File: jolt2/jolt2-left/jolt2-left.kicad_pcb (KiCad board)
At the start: 2 copper layers, 147 x 98 mm, 62 parts, among them J1 Conn_01x02_Pin, J10 Conn_01x02_Pin, J11 Conn_01x02_Pin, J12 Conn_01x02_Pin, J13 Conn_01x02_Pin, J14 Conn_01x02_Pin, J15 Conn_01x02_Pin, J16 Conn_01x02_Pin, J17 Conn_01x02_Pin, J18 Conn_01x02_Pin, J19 Conn_01x02_Pin, J2 Conn_01x02_Pin, J20 Conn_01x02_Pin, J21 Conn_01x02_Pin, J22 Conn_01x02_Pin, J23 Conn_01x02_Pin, J24 Conn_01x02_Pin, J25 Conn_01x02_Pin, J26 Conn_01x02_Pin, J27 Conn_01x02_Pin, J28 Conn_01x02_Pin, J29 USB_C_Receptacle_USB2.0_14P, J3 Conn_01x02_Pin, J30 Conn_ARM_JTAG_SWD_10, J4 Conn_01x02_Pin, J5 Conn_01x02_Pin, J6 Conn_01x02_Pin, J7 Conn_01x02_Pin, J8 Conn_01x02_Pin, J9 Conn_01x02_Pin, SW1 SW_SPST, SW2 SW_SPST, U1 RP2040, U3 W25Q128JVP, Y1 ABM8-272-T3

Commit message: jolt2: Prepare rev A
This is Rev A, being sent for production.
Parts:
- added J31: RJ45, Connector_RJ:RJ45_Amphenol_54602-x08_Horizontal, F.Cu at (173.8, 138.0)
- J29: footprint Connector_USB:USB_C_Receptacle_GCT_USB4085 -> davidb-keyboard-foot:USB_C_Receptacle_GCT_USB4085
- moved J30 12.8 mm to (177.2, 148.6)
- moved C9 3.30 mm to (171.5, 124.2)
- moved C11 0.40 mm to (157.1, 123.5)
- moved R3 0.10 mm to (157.1, 107.5)
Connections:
- U1 pad 2: /COL-A -> /COL-C
- U1 pad 4: /COL-C -> /COL-A
- U1 pad 40: unconnected-(U1-GPIO28_ADC2-Pad40) -> SERTX
- U1 pad 41: unconnected-(U1-GPIO29_ADC3-Pad41) -> SERRX
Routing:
- net /ROW-A: track 0.00 -> 228.4 mm, vias 0 -> 1
- net /ROW-D: track 0.00 -> 153.2 mm, vias 0 -> 2
- net /ROW-B: track 0.00 -> 145.6 mm
- net /ROW-C: track 0.00 -> 143.6 mm
- net /COL-A: track 0.00 -> 139.6 mm
- net /ROW-F: track 0.00 -> 120.1 mm, vias 0 -> 1
- net /ROW-E: track 0.00 -> 110.0 mm, vias 0 -> 2
- net /COL-B: track 0.00 -> 109.6 mm
- net /COL-C: track 0.00 -> 87.3 mm
- net +3.3V: track 103.3 -> 162.2 mm, vias 4 -> 8
- net RUN: track 18.6 -> 74.7 mm, vias 2 -> 4
- net /COL-D: track 0.00 -> 49.1 mm, vias 0 -> 1
- net VBUS: track 7.49 -> 51.5 mm, vias 0 -> 1
- net SERRX: track 0.00 -> 19.9 mm, vias 0 -> 1
- net SERTX: track 0.00 -> 15.7 mm, vias 0 -> 1
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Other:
- board size 147 x 98 mm -> 151 x 98 mm
- board text added: "Jolt 2 - Left REV A"

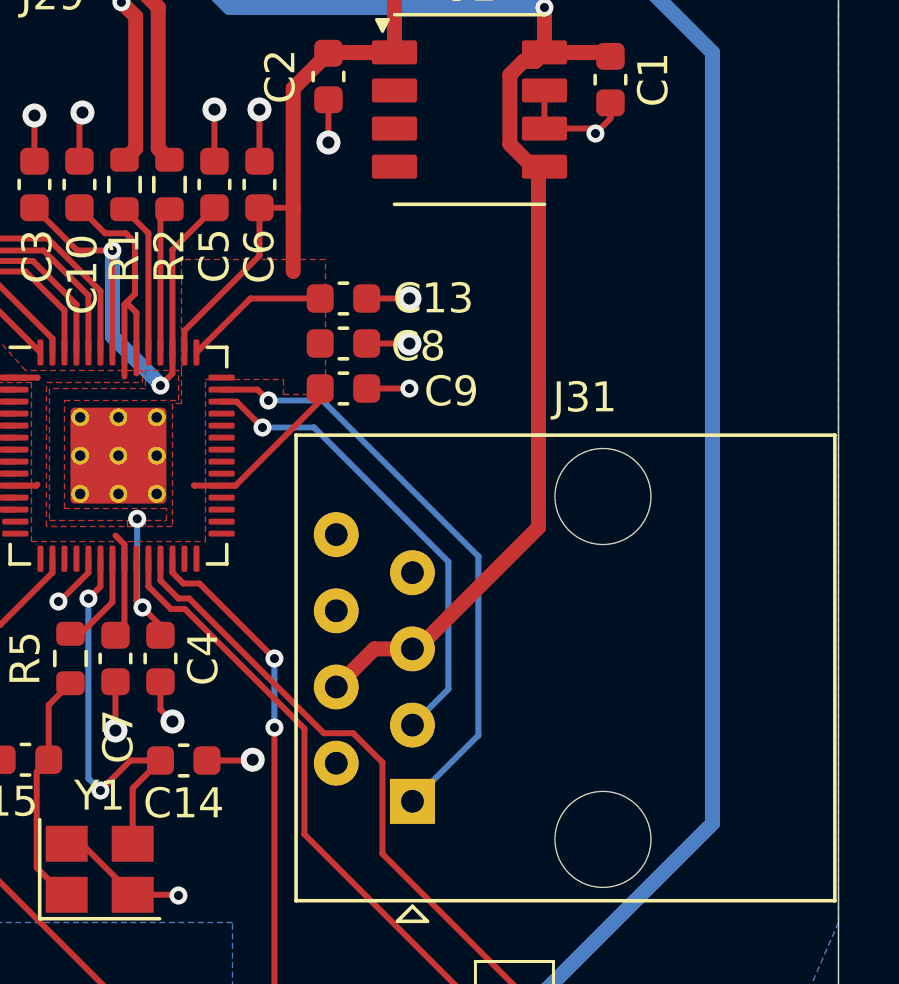
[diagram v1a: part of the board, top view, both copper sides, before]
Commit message: jolt2-left: Add inter-board termination
Add 27 ohm resisters for termination on the inter-board protocol.
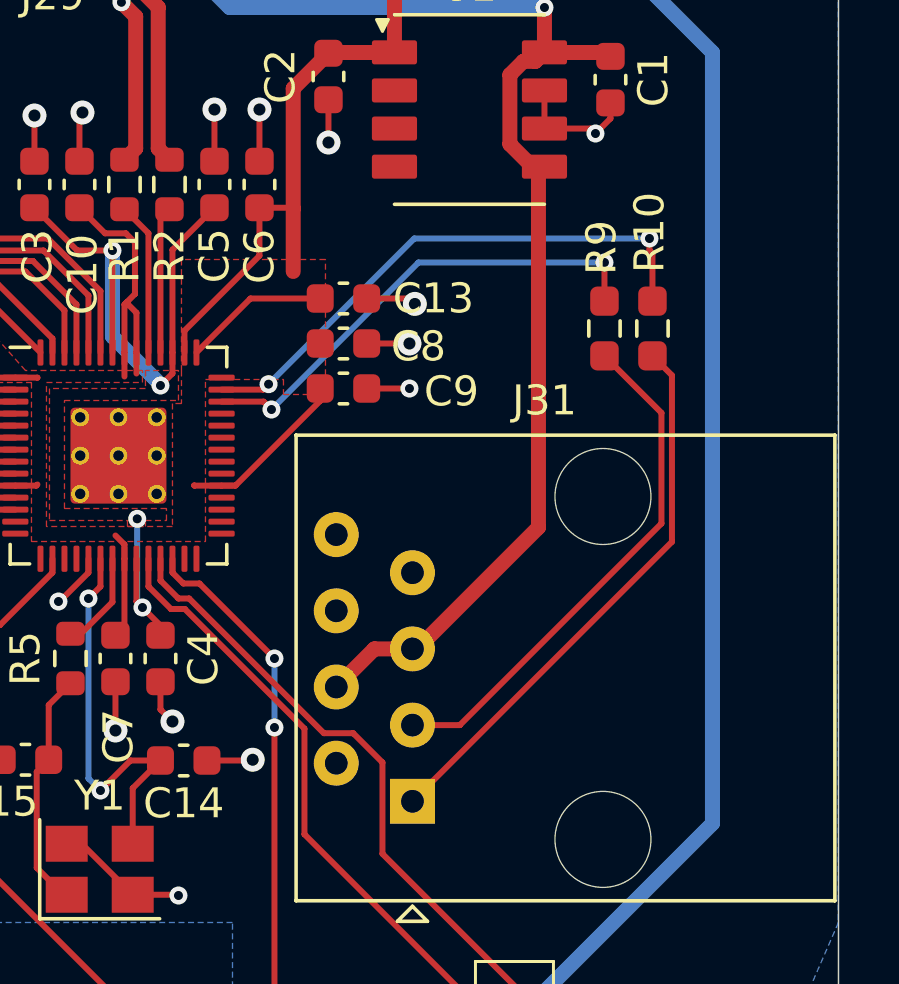
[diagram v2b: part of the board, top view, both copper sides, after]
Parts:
- added R10: 27, Resistor_SMD:R_0603_1608Metric_Pad0.98x0.95mm_HandSolder, F.Cu at (181.8, 122.2)
- added R9: 27, Resistor_SMD:R_0603_1608Metric_Pad0.98x0.95mm_HandSolder, F.Cu at (180.2, 122.2)
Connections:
- J31 pad 1: SERRX -> Net-(J31-Pad1)
- J31 pad 3: SERTX -> Net-(J31-Pad3)
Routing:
- net Net-(J31-Pad1): track 0.00 -> 18.7 mm
- net Net-(J31-Pad3): track 0.00 -> 17.5 mm
- net SERRX: track 19.9 -> 18.5 mm, vias 1 -> 2
- net SERTX: track 15.7 -> 16.2 mm, vias 1 -> 2

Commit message: Various PCB updates
This is before fixing the footprint for the WS2812. Turns out there is a
ws2812 MINI, and a MINI-HS, and they have very different footprints.
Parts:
- C14, C15: value 1u -> 12p
- C16: value C -> 100n
- R3, R4: value R -> 5.1k
- U2: value ~ -> AP2112-M3.3

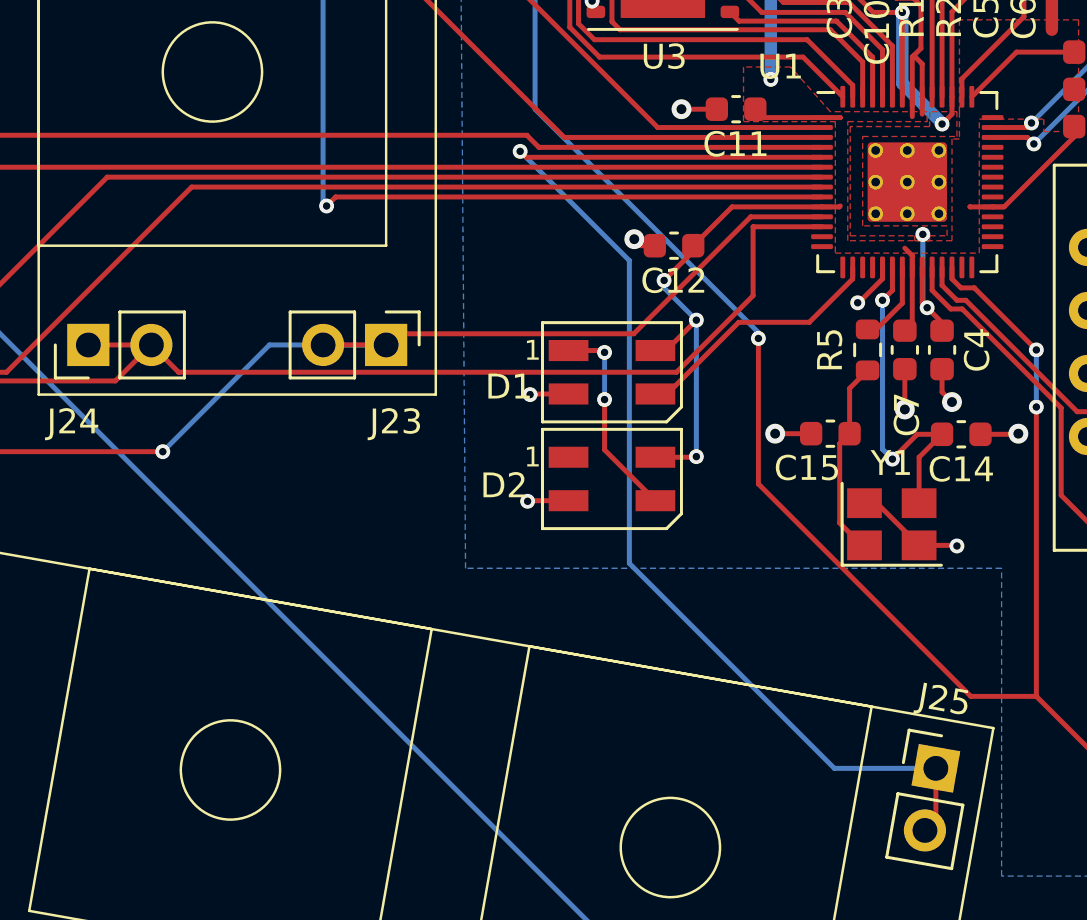
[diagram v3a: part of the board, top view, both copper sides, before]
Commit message: jolt2-left: Fix symbol and footprint for ws2812
The ws2812 has both a MINI and a MINI-HS footprint, and they have rather
different footprints.  Update the symbol and draw a footprint for the
proper one we have purchased.
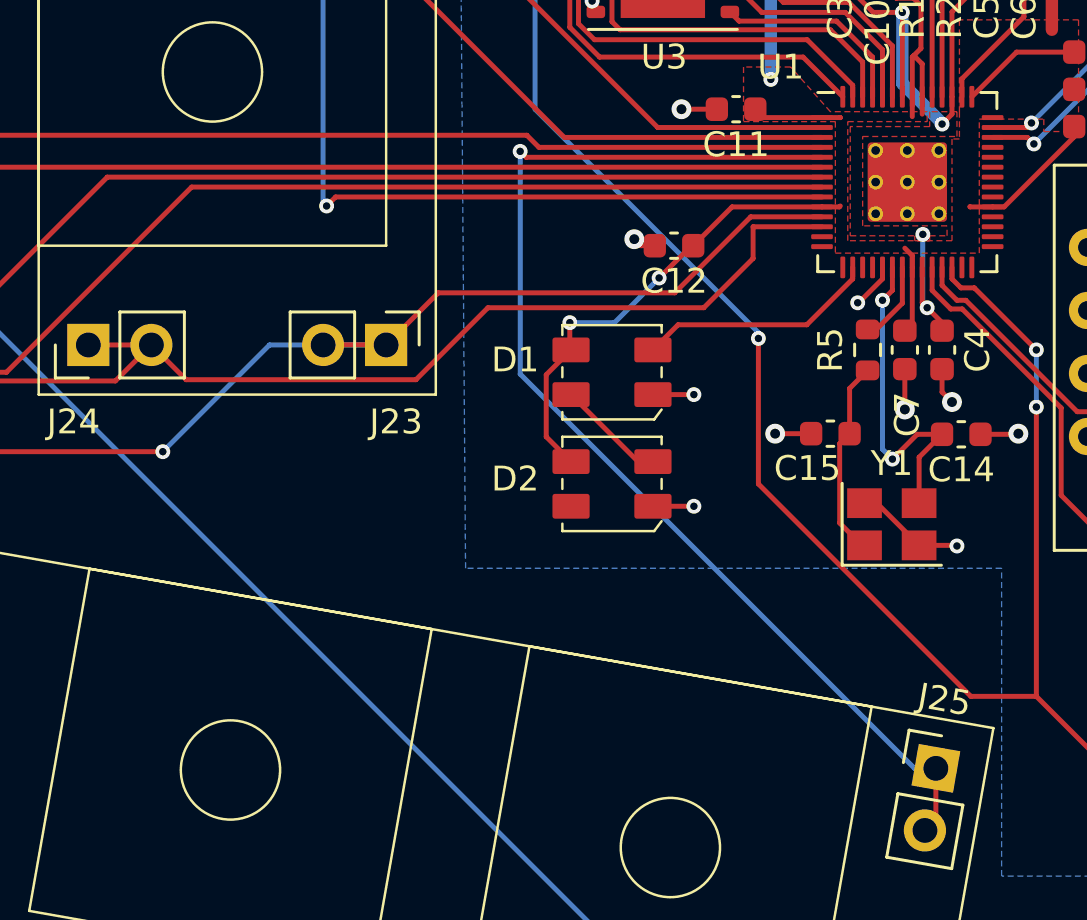
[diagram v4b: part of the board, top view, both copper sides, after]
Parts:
- D1, D2: value SK6812MINI -> SK6812MINI-HS; footprint LED_SMD:LED_SK6812MINI_PLCC4_3.5x3.5mm_P1.75mm -> davidb-keyboard-foot:SK6812-MINI-HS
- moved D2 0.20 mm to (152.1, 138.6), turned to 180 degrees
- turned D1 to 180 degrees
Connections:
- D1 pad 1: Net-(D1-DOUT) -> GND
- D1 pad 2: GND -> RGB
- D1 pad 3: RGB -> +3.3V
- D1 pad 4: +3.3V -> Net-(D1-DOUT)
- D2 pad 1: unconnected-(D2-DOUT-Pad1) -> GND
- D2 pad 2: GND -> Net-(D1-DOUT)
- D2 pad 3: Net-(D1-DOUT) -> +3.3V
- D2 pad 4: +3.3V -> unconnected-(D2-DOUT-Pad4)
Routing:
- net Net-(D1-DOUT): track 8.31 -> 4.42 mm, vias 2 -> 0
- net /COL-D: track 49.1 -> 47.2 mm
- net RGB: track 10.3 -> 9.70 mm
- net +3.3V: track 162.2 -> 161.6 mm, vias 8 -> 7
- net /ROW-F: track 120.1 -> 119.4 mm
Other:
- board text added: "Jolt 2 - Left REV B"
- board text removed: "Jolt 2 - Left REV A"
